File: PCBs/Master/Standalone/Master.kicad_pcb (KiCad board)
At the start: 2 copper layers, 75.4 x 56.3 mm, 76 parts, among them J2 AVR-ISP-6, J3 USB_B_Micro, SW1 SW_MEC_5E, U13 MAX487ESA+T, U14 MAX487ESA+T, U19 MAX487ESA+T, U2 ATmega2560-16A, U20 MAX487ESA+T, U3 CH340C, U7 MAX487ESA+T, U8 MAX487ESA+T, Y1 Crystal_GND24

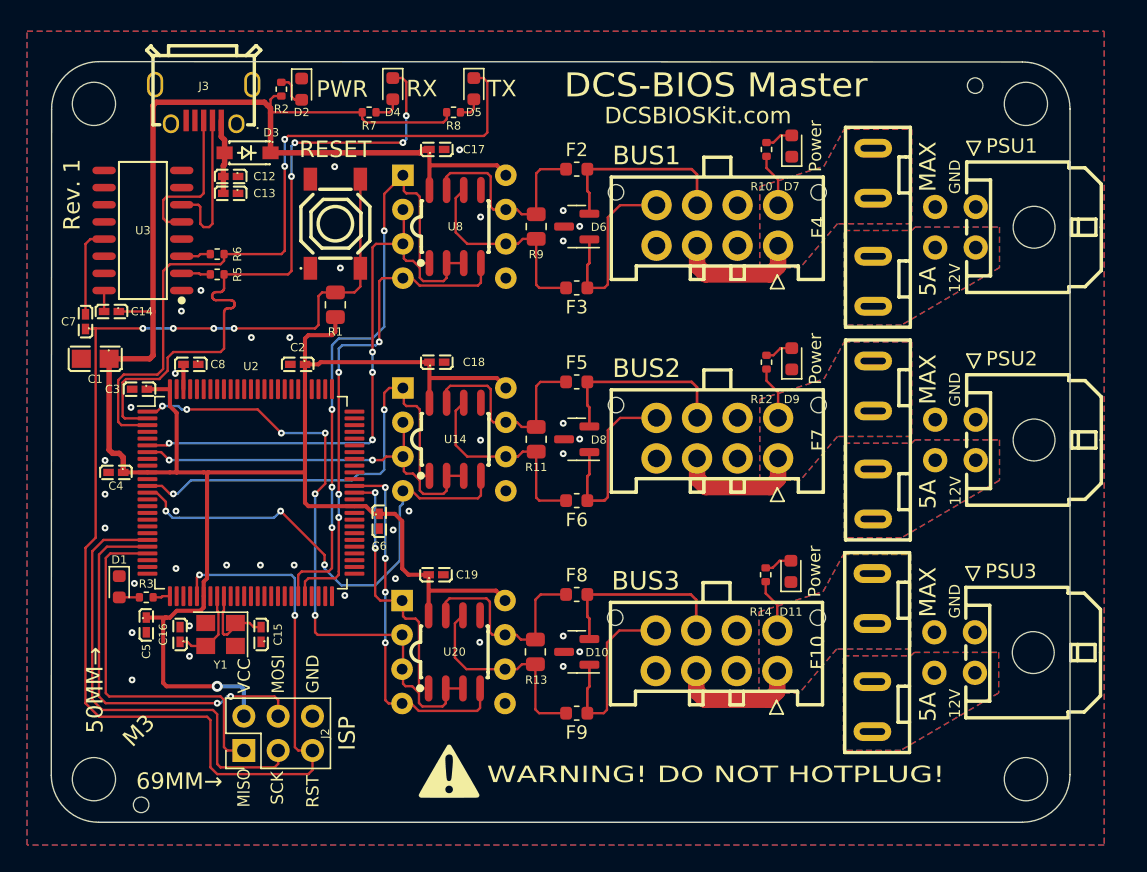
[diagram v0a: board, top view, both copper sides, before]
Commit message: Updated Master to use PCIe Power Directly
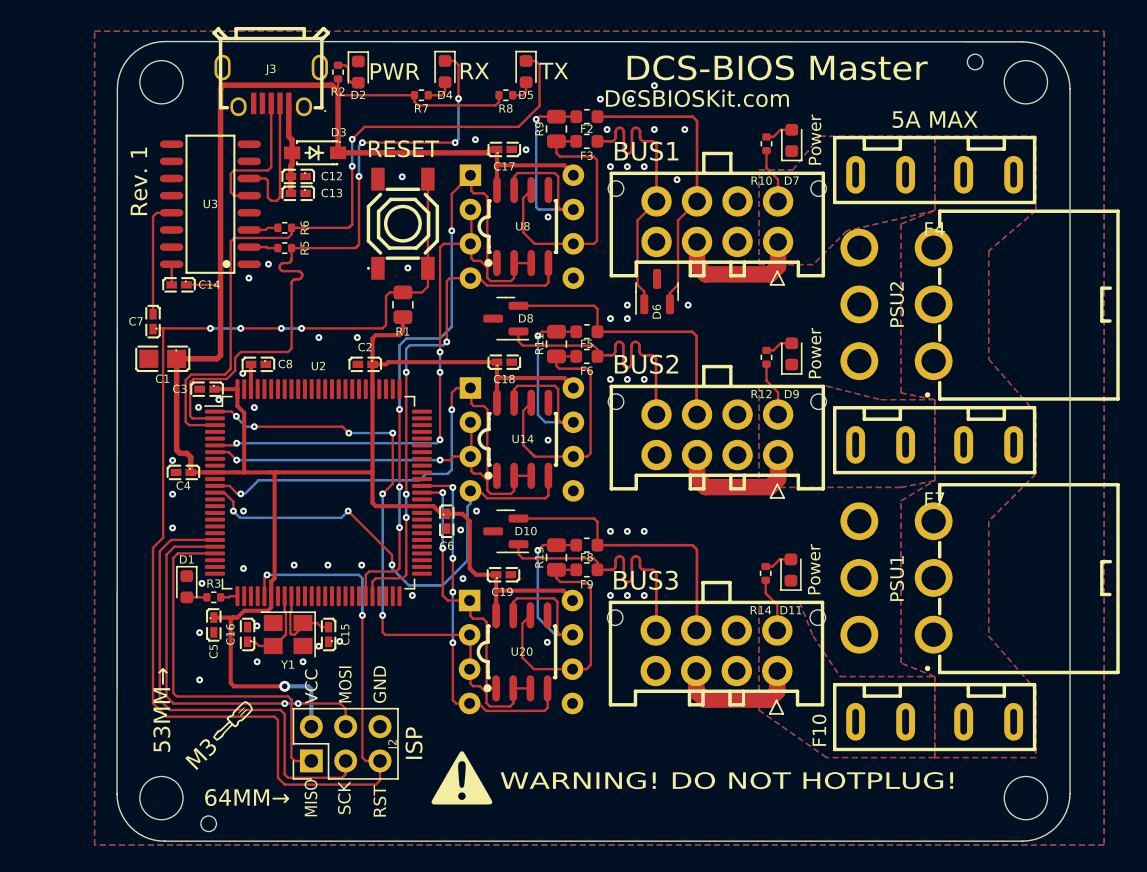
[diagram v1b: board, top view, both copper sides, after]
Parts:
- removed PSU3: Conn_02x02_Top_Bottom, A10 KiCad Libraries:Molex Micro-Fit 3.0 43045-0400
- added G***: LOGO, LOGO, F.Cu at (110.0, 115.2)
- PSU1, PSU2: value Conn_02x02_Top_Bottom -> Conn_02x03_Odd_Even; footprint A10 KiCad Libraries:Molex Micro-Fit 3.0 43045-0400 -> A10 KiCad Libraries:CONN-TH_HAA420A-6AW-C2845788
- moved PSU1 26.0 mm to (166.0, 104.8)
- moved F3 10.9 mm to (136.2, 72.4)
- moved F6 10.7 mm to (136.2, 88.3)
- moved F9 10.6 mm to (136.2, 104.1)
- moved D8 10.4 mm to (130.2, 85.5)
- moved D10 10.4 mm to (130.2, 101.2)
- moved PSU2 10.0 mm to (166.0, 84.5)
- moved D6 7.65 mm to (141.4, 83.5), turned to 90 degrees
- moved R9 7.38 mm to (134.0, 71.5)
- moved R11 7.21 mm to (134.0, 87.4)
- moved R13 7.16 mm to (134.0, 103.2)
- moved F10 6.40 mm to (162.0, 115.0), turned to 180 degrees
- moved F4 5.96 mm to (162.0, 74.5), turned to 180 degrees
- moved G*** 5.72 mm to (138.0, 92.6)
- moved C14 5.38 mm to (106.1, 83.0)
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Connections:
- F10 pad 1: Net-(F10-Pad1) -> +12V
- F4 pad 1: Net-(F4-Pad1) -> +12V
- F7 pad 1: Net-(F7-Pad1) -> +12V
- PSU1 pad 1: GND -> +12V
- PSU1 pad 2: Net-(F4-Pad1) -> GND
- PSU1 pad 3: GND -> +12V
- PSU1 pad 4: Net-(F4-Pad1) -> GND
- PSU2 pad 1: GND -> +12V
- PSU2 pad 2: Net-(F7-Pad1) -> GND
- PSU2 pad 3: GND -> +12V
- PSU2 pad 4: Net-(F7-Pad1) -> GND
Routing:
- net RS485-1-: track 13.9 -> 21.9 mm
- net RS485-1+: track 14.2 -> 21.8 mm
- net RS485-3-: track 13.9 -> 21.1 mm
- net RS485-2-: track 13.9 -> 21.1 mm
- net RS485-3+: track 14.2 -> 20.7 mm
- net RS485-2+: track 14.2 -> 20.7 mm
- net Net-(F3-Pad2): track 15.6 -> 20.8 mm
- net Net-(F2-Pad1): track 15.7 -> 20.3 mm, vias 0 -> 1
- net Net-(F6-Pad2): track 15.6 -> 20.1 mm
- net Net-(F9-Pad2): track 15.6 -> 19.6 mm
- net Net-(F5-Pad1): track 15.7 -> 19.6 mm, vias 0 -> 1
- net Net-(F8-Pad1): track 15.7 -> 19.0 mm, vias 0 -> 1
- net FTDI_DTR: track 6.73 -> 8.72 mm
- net RESET: track 104.2 -> 105.8 mm
- net Net-(C12-Pad2): track 5.54 -> 6.81 mm
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- added copper zone on B.Cu, net +12V
- added copper zone on F.Cu, net +12V
- removed copper zone on B.Cu, net Net-(F10-Pad1)
- removed copper zone on F.Cu, net Net-(F10-Pad1)
- removed copper zone on B.Cu, net Net-(F4-Pad1)
- removed copper zone on F.Cu, net Net-(F4-Pad1)
- removed copper zone on B.Cu, net Net-(F7-Pad1)
- removed copper zone on F.Cu, net Net-(F7-Pad1)
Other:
- board size 75.4 x 56.3 mm -> 70.6 x 59.2 mm
- board text added: "53MM→"
- board text added: "64MM→"
- board text removed: "50MM→"
- board text removed: "69MM→"
